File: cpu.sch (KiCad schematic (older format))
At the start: 26 parts, among them SW1 RESET, U1 74HC04, U2 Z80CPU, Y1 7.3728MHz

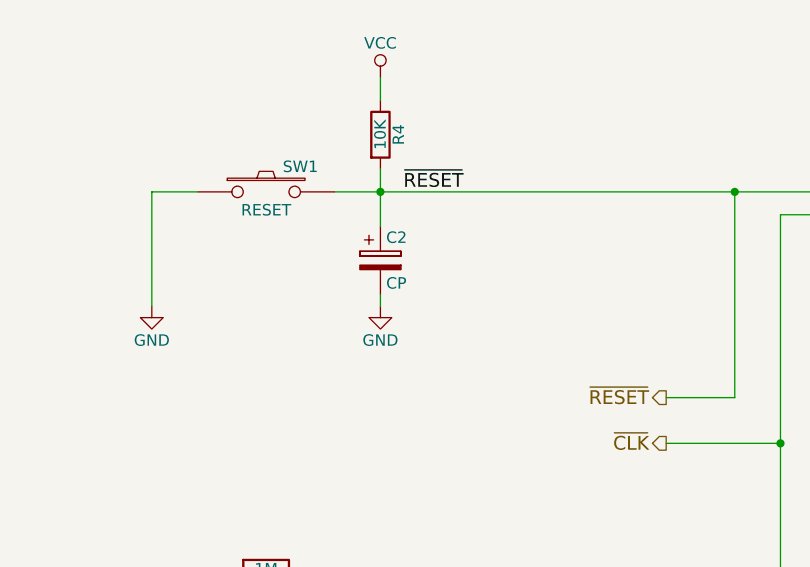
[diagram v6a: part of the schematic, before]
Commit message: Added missing signals to IO and added buffer
I've removed the /WAIT and also added a somewhat dodgy diode AND to
handle the bi-directional Dx buffer. Might work, might not.

Also cleaned up the buses and just tidied things up.
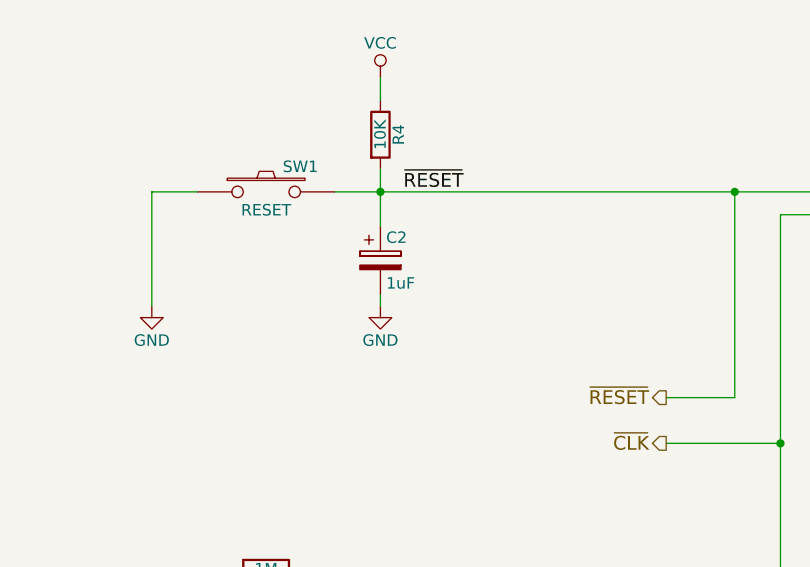
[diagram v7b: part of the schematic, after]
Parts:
- C2: value CP -> 1uF
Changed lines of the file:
@@
 	9650 4700 9300 4700
 $Comp
-L VCC #PWR01
+L VCC #PWR9
 U 1 1 577A5457
 P 6500 3100
-F 0 "#PWR01" H 6500 2950 50  0001 C CNN
+F 0 "#PWR9" H 6500 2950 50  0001 C CNN
 F 1 "VCC" H 6500 3250 50  0000 C CNN
 F 2 "" H 6500 3100 50  0000 C CNN
@@
 $EndComp
 $Comp
-L VCC #PWR02
+L VCC #PWR10
 U 1 1 577A54A8
 P 6700 1850
-F 0 "#PWR02" H 6700 1700 50  0001 C CNN
+F 0 "#PWR10" H 6700 1700 50  0001 C CNN
 F 1 "VCC" H 6700 2000 50  0000 C CNN
 F 2 "" H 6700 1850 50  0000 C CNN
@@
 	8250 1550 8250 750
 $Comp
-L VCC #PWR03
+L VCC #PWR11
 U 1 1 577A54FB
 P 8250 750
-F 0 "#PWR03" H 8250 600 50  0001 C CNN
+F 0 "#PWR11" H 8250 600 50  0001 C CNN
 F 1 "VCC" H 8250 900 50  0000 C CNN
 F 2 "" H 8250 750 50  0000 C CNN
@@
 	8250 4550 8250 4700
 $Comp
-L GND #PWR04
+L GND #PWR12
 U 1 1 577A554F
 P 8250 4700
-F 0 "#PWR04" H 8250 4450 50  0001 C CNN
+F 0 "#PWR12" H 8250 4450 50  0001 C CNN
 F 1 "GND" H 8250 4550 50  0000 C CNN
 F 2 "" H 8250 4700 50  0000 C CNN
@@
 	4050 4700 4050 4900
 $Comp
-L GND #PWR05
+L GND #PWR3
 U 1 1 577B2CBE
 P 3050 4900
-F 0 "#PWR05" H 3050 4650 50  0001 C CNN
+F 0 "#PWR3" H 3050 4650 50  0001 C CNN
 F 1 "GND" H 3050 4750 50  0000 C CNN
 F 2 "" H 3050 4900 50  0000 C CNN
@@
 $EndComp
 $Comp
-L GND #PWR06
+L GND #PWR7
 U 1 1 577B2D0B
 P 4050 4900
-F 0 "#PWR06" H 4050 4650 50  0001 C CNN
+F 0 "#PWR7" H 4050 4650 50  0001 C CNN
 F 1 "GND" H 4050 4750 50  0000 C CNN
 F 2 "" H 4050 4900 50  0000 C CNN
@@
 $EndComp
 $Comp
-L GND #PWR07
+L GND #PWR4
 U 1 1 577B377E
 P 3750 7000
-F 0 "#PWR07" H 3750 6750 50  0001 C CNN
+F 0 "#PWR4" H 3750 6750 50  0001 C CNN
 F 1 "GND" H 3750 6850 50  0000 C CNN
 F 2 "" H 3750 7000 50  0000 C CNN
@@
 	3050 1400 3050 1900
 $Comp
-L GND #PWR08
+L GND #PWR2
 U 1 1 577B455D
 P 3050 1900
-F 0 "#PWR08" H 3050 1650 50  0001 C CNN
+F 0 "#PWR2" H 3050 1650 50  0001 C CNN
 F 1 "GND" H 3050 1750 50  0000 C CNN
 F 2 "" H 3050 1900 50  0000 C CNN
@@
 P 4050 1700
 F 0 "C2" H 4075 1800 50  0000 L CNN
-F 1 "CP" H 4075 1600 50  0000 L CNN
+F 1 "1uF" H 4075 1600 50  0000 L CNN
 F 2 "Capacitors_ThroughHole:C_Radial_D6.3_L11.2_P2.5" H 4088 1550 50  0001 C CNN
 F 3 "" H 4050 1700 50  0000 C CNN
@@
 	4050 1850 4050 1900
 $Comp
-L GND #PWR09
+L GND #PWR6
 U 1 1 577B48FE
 P 4050 1900
-F 0 "#PWR09" H 4050 1650 50  0001 C CNN
+F 0 "#PWR6" H 4050 1650 50  0001 C CNN
 F 1 "GND" H 4050 1750 50  0000 C CNN
 F 2 "" H 4050 1900 50  0000 C CNN
@@
 $EndComp
 $Comp
-L GND #PWR010
+L GND #PWR1
 U 1 1 577B4B0C
 P 1850 7000
-F 0 "#PWR010" H 1850 6750 50  0001 C CNN
+F 0 "#PWR1" H 1850 6750 50  0001 C CNN
 F 1 "GND" H 1850 6850 50  0000 C CNN
 F 2 "" H 1850 7000 50  0000 C CNN
@@
 $EndComp
 $Comp
-L VCC #PWR011
+L VCC #PWR5
 U 1 1 577B4D04
 P 4050 900
-F 0 "#PWR011" H 4050 750 50  0001 C CNN
+F 0 "#PWR5" H 4050 750 50  0001 C CNN
 F 1 "VCC" H 4050 1050 50  0000 C CNN
 F 2 "" H 4050 900 50  0000 C CNN
@@
 $EndComp
 $Comp
-L GND #PWR012
+L GND #PWR8
 U 1 1 577B52BF
 P 5700 7000
-F 0 "#PWR012" H 5700 6750 50  0001 C CNN
+F 0 "#PWR8" H 5700 6750 50  0001 C CNN
 F 1 "GND" H 5700 6850 50  0000 C CNN
 F 2 "" H 5700 7000 50  0000 C CNN
@@
 Connection ~ 8600 750
 $Comp
-L GND #PWR013
+L GND #PWR13
 U 1 1 577B59DE
 P 8600 1250
-F 0 "#PWR013" H 8600 1000 50  0001 C CNN
+F 0 "#PWR13" H 8600 1000 50  0001 C CNN
 F 1 "GND" H 8600 1100 50  0000 C CNN
 F 2 "" H 8600 1250 50  0000 C CNN
@@
 $EndComp
 $Comp
-L GND #PWR014
+L GND #PWR14
 U 1 1 577B5A43
 P 9000 1250
-F 0 "#PWR014" H 9000 1000 50  0001 C CNN
+F 0 "#PWR14" H 9000 1000 50  0001 C CNN
 F 1 "GND" H 9000 1100 50  0000 C CNN
 F 2 "" H 9000 1250 50  0000 C CNN
@@
 ~RESET
 $Comp
-L PWR_FLAG #FLG015
+L PWR_FLAG #FLG2
 U 1 1 5780650C
 P 9000 750
-F 0 "#FLG015" H 9000 845 50  0001 C CNN
+F 0 "#FLG2" H 9000 845 50  0001 C CNN
 F 1 "PWR_FLAG" H 9000 930 50  0000 C CNN
 F 2 "" H 9000 750 50  0000 C CNN
@@
 $EndComp
 $Comp
-L PWR_FLAG #FLG016
+L PWR_FLAG #FLG1
 U 1 1 57806779
 P 8550 4650
-F 0 "#FLG016" H 8550 4745 50  0001 C CNN
+F 0 "#FLG1" H 8550 4745 50  0001 C CNN
 F 1 "PWR_FLAG" H 8550 4830 50  0000 C CNN
 F 2 "" H 8550 4650 50  0000 C CNN
